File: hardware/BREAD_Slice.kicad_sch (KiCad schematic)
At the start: 15 parts, among them J1 Conn_01x10_Female, J2 I2C_01x04

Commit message: Initial commit
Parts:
- removed C1, C3, C4: 22uF, Capacitor_SMD:C_1206_3216Metric, symbol Device:C_Small
- removed C2: 100nF, Capacitor_SMD:C_1206_3216Metric, symbol Device:C_Small
- removed D1: WS2812B_5050, SparkFun-LED:WS2812-5050-4PIN, symbol SparkFun-LED:WS2812B_5050
- removed HS1: Heatsink_Pad, SparkFun-Fuse:Thermal Pad, symbol Mechanical:Heatsink_Pad
- removed J2: I2C_01x04, Connector_JST:JST_SH_SM04B-SRSS-TB_1x04-1MP_P1.00mm_Horizontal, symbol SparkFun-Connector:I2C_01x04
- removed L1: 4.7uH, Inductor_SMD:L_1210_3225Metric, symbol Device:L_Small
- removed U1: ~, Package_TO_SOT_SMD:TSOT-23-6, symbol SparkFun-DiscreteSemi:AP63205
- added C1, C2: 10uF_t, OCI_UPL_FOOTPRINTS:C_2312, symbol BREAD_Slice-rescue:10uF_t-OCI_UPL_2_Capacitors
- added C3: 0.01 uF, OCI_UPL_FOOTPRINTS:C_1206_HandSoldering, symbol Device:C
- added FB1, FB2: Ferrite_Bead_Small, OCI_UPL_FOOTPRINTS:R_1206_HandSoldering, symbol BREAD_Slice-rescue:Ferrite_Bead_Small-Device
- added J2, J3, J4: Screw_Terminal_01x02, OCI_UPL_FOOTPRINTS:TerminalBlock_Pheonix_MKDS1.5-2pol, symbol Connector:Screw_Terminal_01x02
- added Logo1: Logo_Open_Hardware_Small, Symbol:OSHW-Symbol_6.7x6mm_SilkScreen, symbol Graphic:Logo_Open_Hardware_Small
- added Q1, Q2: TIP120, Package_TO_SOT_THT:TO-220-3_Vertical, symbol Transistor_BJT:TIP120
- added R1, R2, R3: 10k, OCI_UPL_FOOTPRINTS:R_1206_HandSoldering, symbol Device:R_US
- added U1: MAX31855KASA, Package_SO:SOIC-8_3.9x4.9mm_P1.27mm, symbol BREAD_Slice-rescue:MAX31855KASA-Sensor_Temperature
- H1, H4: footprint MountingHole:MountingHole_5mm -> MountingHole:MountingHole_3.2mm_M3_DIN965_Pad
- H2: renamed from H3; footprint MountingHole:MountingHole_5mm -> MountingHole:MountingHole_3.2mm_M3_DIN965_Pad
- H3: renamed from H2; footprint MountingHole:MountingHole_5mm -> MountingHole:MountingHole_3.2mm_M3_DIN965_Pad
- J1: symbol Connector:Conn_01x10_Female -> BREAD_Slice-rescue:Conn_01x10_Female-Connector
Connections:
- net +12V: now also A1.30 (VIN), C1.1, Q2.2 (C)
- net +5V: now also C2.1, R1.1, R2.2, R3.1, U1.4 (VCC)
- net E_STOP: now also Q2.1 (B)
- net GND: now also C1.2, C2.2, J4.2 (Pin_2), Q1.3 (E), U1.1 (GND)
- net SS: now reaches A1.12 (D9)
- net SS: now also R2.1, U1.6 (~{CS})
- net DATA: now reaches A1.13 (D10)
- net DATA: now also U1.7 (SO)
- net CLK: now reaches A1.14 (D11)
- net CLK: now also R3.2, U1.5 (SCK)
- net TMSTR: now reaches A1.19 (A0)
- net TMSTR: now also J4.1 (Pin_1), R1.2
- net PWM: now reaches A1.9 (D6)
- net PWM: now also Q1.1 (B)
- net LED: no longer names the net of A1.8 (D5)
- new net: J3.2 (Pin_2), Q1.2 (C)
- new net: J3.1 (Pin_1), Q2.3 (E)
- new net: FB2.2, J2.1 (Pin_1)
- new net: FB1.2, J2.2 (Pin_2)
- new net: C3.1, FB1.1, U1.3 (T+)
- new net: C3.2, FB2.1, U1.2 (T-)
- no-connect marks 22 -> 16
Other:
- moved on the sheet: A1, H1, H2, H3, H4, J1

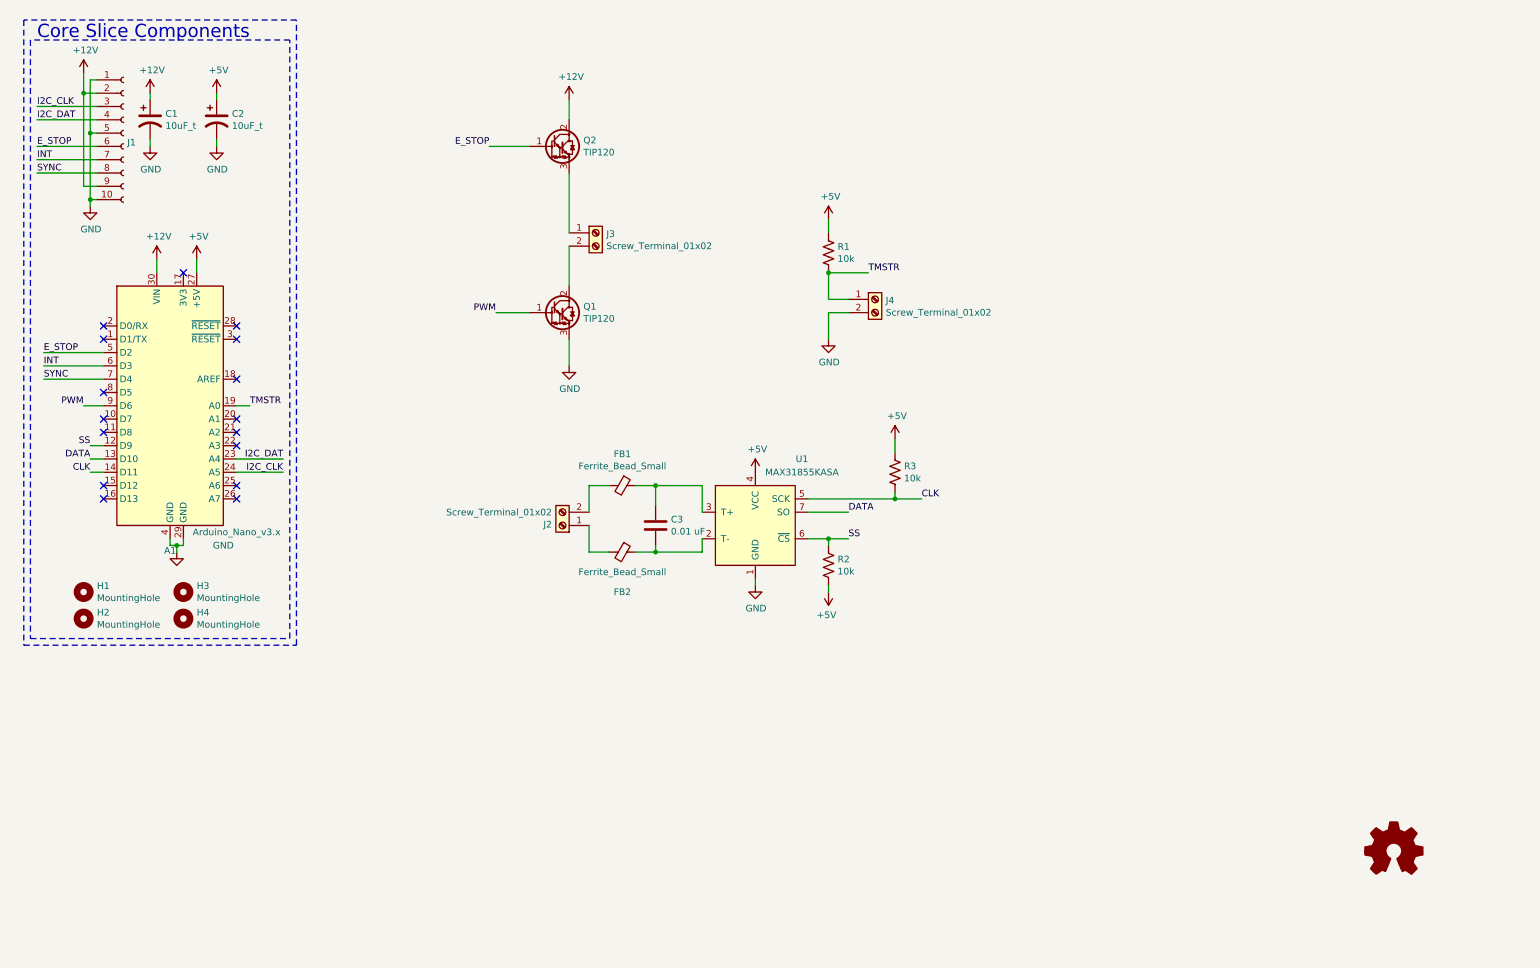
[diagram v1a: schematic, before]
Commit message: upgraded by duplicating ciruit, new core, all back copper
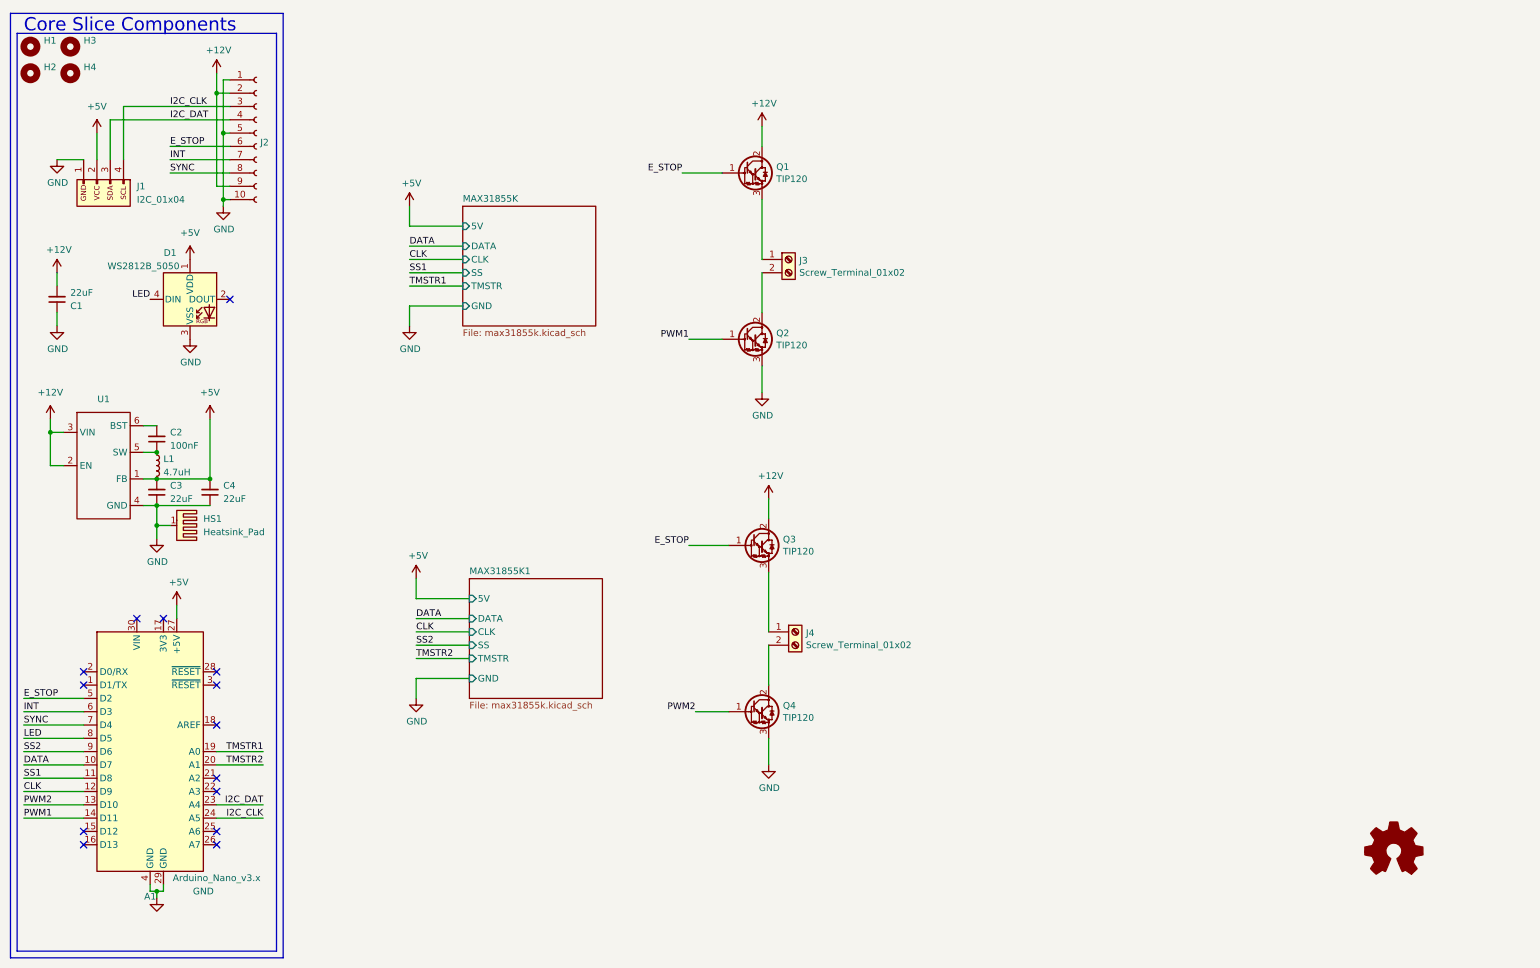
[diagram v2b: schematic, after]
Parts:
- removed C1, C2: 10uF_t, OCI_UPL_FOOTPRINTS:C_2312, symbol BREAD_Slice-rescue:10uF_t-OCI_UPL_2_Capacitors
- removed C3: 0.01 uF, OCI_UPL_FOOTPRINTS:C_1206_HandSoldering, symbol Device:C
- removed FB1, FB2: Ferrite_Bead_Small, OCI_UPL_FOOTPRINTS:R_1206_HandSoldering, symbol BREAD_Slice-rescue:Ferrite_Bead_Small-Device
- removed J2: Screw_Terminal_01x02, OCI_UPL_FOOTPRINTS:TerminalBlock_Pheonix_MKDS1.5-2pol, symbol Connector:Screw_Terminal_01x02
- removed Logo1: Logo_Open_Hardware_Small, Symbol:OSHW-Symbol_6.7x6mm_SilkScreen, symbol Graphic:Logo_Open_Hardware_Small
- removed R1, R2, R3: 10k, OCI_UPL_FOOTPRINTS:R_1206_HandSoldering, symbol Device:R_US
- removed U1: MAX31855KASA, Package_SO:SOIC-8_3.9x4.9mm_P1.27mm, symbol BREAD_Slice-rescue:MAX31855KASA-Sensor_Temperature
- added C1, C3, C4: 22uF, Capacitor_SMD:C_1206_3216Metric, symbol Device:C_Small
- added C2: 100nF, Capacitor_SMD:C_1206_3216Metric, symbol Device:C_Small
- added D1: WS2812B_5050, SparkFun-LED:WS2812-5050-4PIN, symbol SparkFun-LED:WS2812B_5050
- added HS1: Heatsink_Pad, KML-Custom:Thermal Pad, symbol Mechanical:Heatsink_Pad
- added J1: I2C_01x04, Connector_JST:JST_SH_SM04B-SRSS-TB_1x04-1MP_P1.00mm_Horizontal, symbol SparkFun-Connector:I2C_01x04
- added L1: 4.7uH, Inductor_SMD:L_1210_3225Metric, symbol Device:L_Small
- added Q3, Q4: TIP120, Package_TO_SOT_THT:TO-220-3_Horizontal_TabUp, symbol Transistor_BJT:TIP120
- added U1: ~, Package_TO_SOT_SMD:TSOT-23-6, symbol SparkFun-DiscreteSemi:AP63205
- H1, H4: footprint MountingHole:MountingHole_3.2mm_M3_DIN965_Pad -> MountingHole:MountingHole_5mm
- H2: renamed from H3; footprint MountingHole:MountingHole_3.2mm_M3_DIN965_Pad -> MountingHole:MountingHole_5mm
- H3: renamed from H2; footprint MountingHole:MountingHole_3.2mm_M3_DIN965_Pad -> MountingHole:MountingHole_5mm
- J2: renamed from J1; symbol BREAD_Slice-rescue:Conn_01x10_Female-Connector -> Connector:Conn_01x10_Female
- J3, J4: footprint OCI_UPL_FOOTPRINTS:TerminalBlock_Pheonix_MKDS1.5-2pol -> TerminalBlock_Phoenix:TerminalBlock_Phoenix_MKDS-1,5-2_1x02_P5.00mm_Horizontal
- Q1, Q2: footprint Package_TO_SOT_THT:TO-220-3_Vertical -> Package_TO_SOT_THT:TO-220-3_Horizontal_TabDown
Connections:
- net SS is gone; now on net CLK: A1.12 (D9)
- net +12V: now also Q1.2 (C), C1.2, Q3.2 (C), U1.2 (EN), U1.3 (VIN); no longer A1.30 (VIN), Q2.2 (C)
- net +5V: now also C3.2, C4.2, D1.1 (VDD), J1.2 (Pin_2), L1.2, U1.1 (FB)
- net CLK: no longer A1.14 (D11)
- net DATA: now also A1.10 (D7); no longer A1.13 (D10)
- net E_STOP: now also Q1.1 (B), Q3.1 (B); no longer Q2.1 (B)
- net GND: now also Q2.3 (E), C1.1, C3.1, C4.1, D1.3 (VSS), HS1.1, J1.1 (Pin_1), Q4.3 (E), U1.4 (GND); no longer J4.2 (Pin_2), Q1.3 (E)
- net I2C_CLK: now also J1.4 (Pin_4)
- net I2C_DAT: now also J1.3 (Pin_3)
- net SS1: now reaches A1.11 (D8)
- net TMSTR2: now reaches A1.20 (A1)
- net LED: now reaches A1.8 (D5)
- net LED: now also D1.4 (DIN)
- net at J3.2 (Pin_2): now also Q2.2 (C); no longer Q1.2 (C)
- net at J3.1 (Pin_1): now also Q1.3 (E); no longer Q2.3 (E)
- net PWM renamed SS2
- net SS2: no longer Q1.1 (B)
- net TMSTR: no longer names the net of J4.1 (Pin_1)
- net TMSTR: now also Q3.3 (E); no longer A1.19 (A0)
- new net: C2.1, L1.1, U1.5 (SW)
- new net: C2.2, U1.6 (BST)
- new net: J4.2 (Pin_2), Q4.2 (C)
- new net PWM1: A1.14 (D11), Q2.1 (B)
- new net PWM2: A1.13 (D10), Q4.1 (B)
- new net TMSTR1: A1.19 (A0)
- no-connect marks 16 -> 14
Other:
- added sheet MAX31855K (max31855k.kicad_sch)
- added sheet MAX31855K1 (max31855k.kicad_sch)
- moved on the sheet: A1, H1, H2, H3, H4, J2

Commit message: updated to the correct terminals and proper hierarchial pages
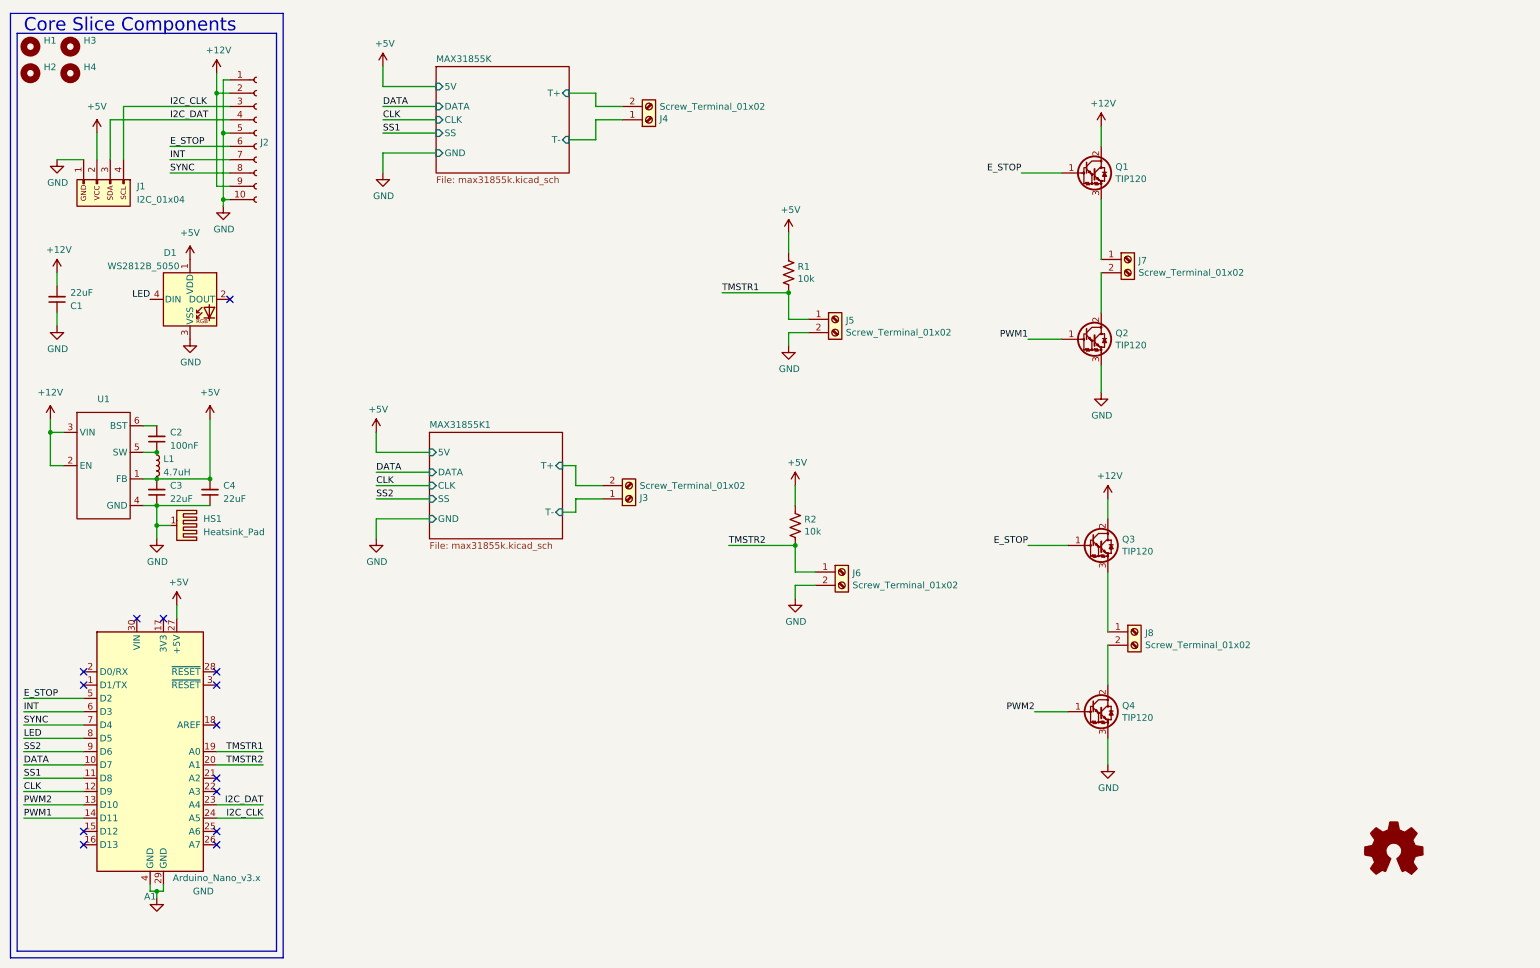
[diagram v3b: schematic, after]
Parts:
- added J3, J4, J5, J6: Screw_Terminal_01x02, TerminalBlock_Phoenix:TerminalBlock_Phoenix_MPT-0,5-2-2.54_1x02_P2.54mm_Horizontal, symbol Connector:Screw_Terminal_01x02
- added R1, R2: 10k, Resistor_SMD:R_1206_3216Metric_Pad1.30x1.75mm_HandSolder, symbol Device:R_US
- renumbered J3 to J7, J4 to J8
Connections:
- net +5V: now also R1.1, R2.1
- net GND: now also J5.2 (Pin_2), J6.2 (Pin_2)
- net TMSTR1: now also J5.1 (Pin_1), R1.2
- net TMSTR2: now also J6.1 (Pin_1), R2.2
- new net MAX31855K/T+: J4.2 (Pin_2)
- new net MAX31855K/T-: J4.1 (Pin_1)
- new net MAX31855K1/T+: J3.2 (Pin_2)
- new net MAX31855K1/T-: J3.1 (Pin_1)
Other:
- sheet MAX31855K ports: added T+, T-; removed TMSTR
- sheet MAX31855K1 ports: added T+, T-; removed TMSTR
- moved on the sheet: J7, J8, Q1, Q2, Q3, Q4

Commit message: JLCPCB order rev-A
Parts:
- removed J3, J4, J5, J6: Screw_Terminal_01x02, TerminalBlock_Phoenix:TerminalBlock_Phoenix_MPT-0,5-2-2.54_1x02_P2.54mm_Horizontal, symbol Connector:Screw_Terminal_01x02
- removed J7, J8: Screw_Terminal_01x02, TerminalBlock_Phoenix:TerminalBlock_Phoenix_MKDS-1,5-2_1x02_P5.00mm_Horizontal, symbol Connector:Screw_Terminal_01x02
- added J10, J11, J12, J13, J14, J3, J4, J5, J6, J7, J8, J9: Term_PressFit_1x01_5mm_Phoenix_Contact_1751066, 1751066, symbol kml-custom:Term_PressFit_1x01_5mm_Phoenix_Contact_1751066
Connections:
- net GND: now also J10.1, J10.2, J8.1, J8.2
- net MAX31855K/T+: now also J3.1, J3.2
- net MAX31855K/T-: now also J4.1, J4.2
- net MAX31855K1/T+: now also J5.1, J5.2
- net MAX31855K1/T-: now also J6.1, J6.2
- net TMSTR1: now also J7.1, J7.2
- net TMSTR2: now also J9.1, J9.2
- net at Q1.3 (E): now also J11.1, J11.2
- net at Q2.2 (C): now also J12.1, J12.2
- net at Q3.3 (E): now also J13.1, J13.2
- net at Q4.2 (C): now also J14.1, J14.2
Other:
- moved on the sheet: R1, R2
